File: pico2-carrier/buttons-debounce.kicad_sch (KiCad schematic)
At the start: 13 parts, among them SW5 BUT_L, SW6 BUT_M, SW7 BUT_R, U6 74HC14_x6

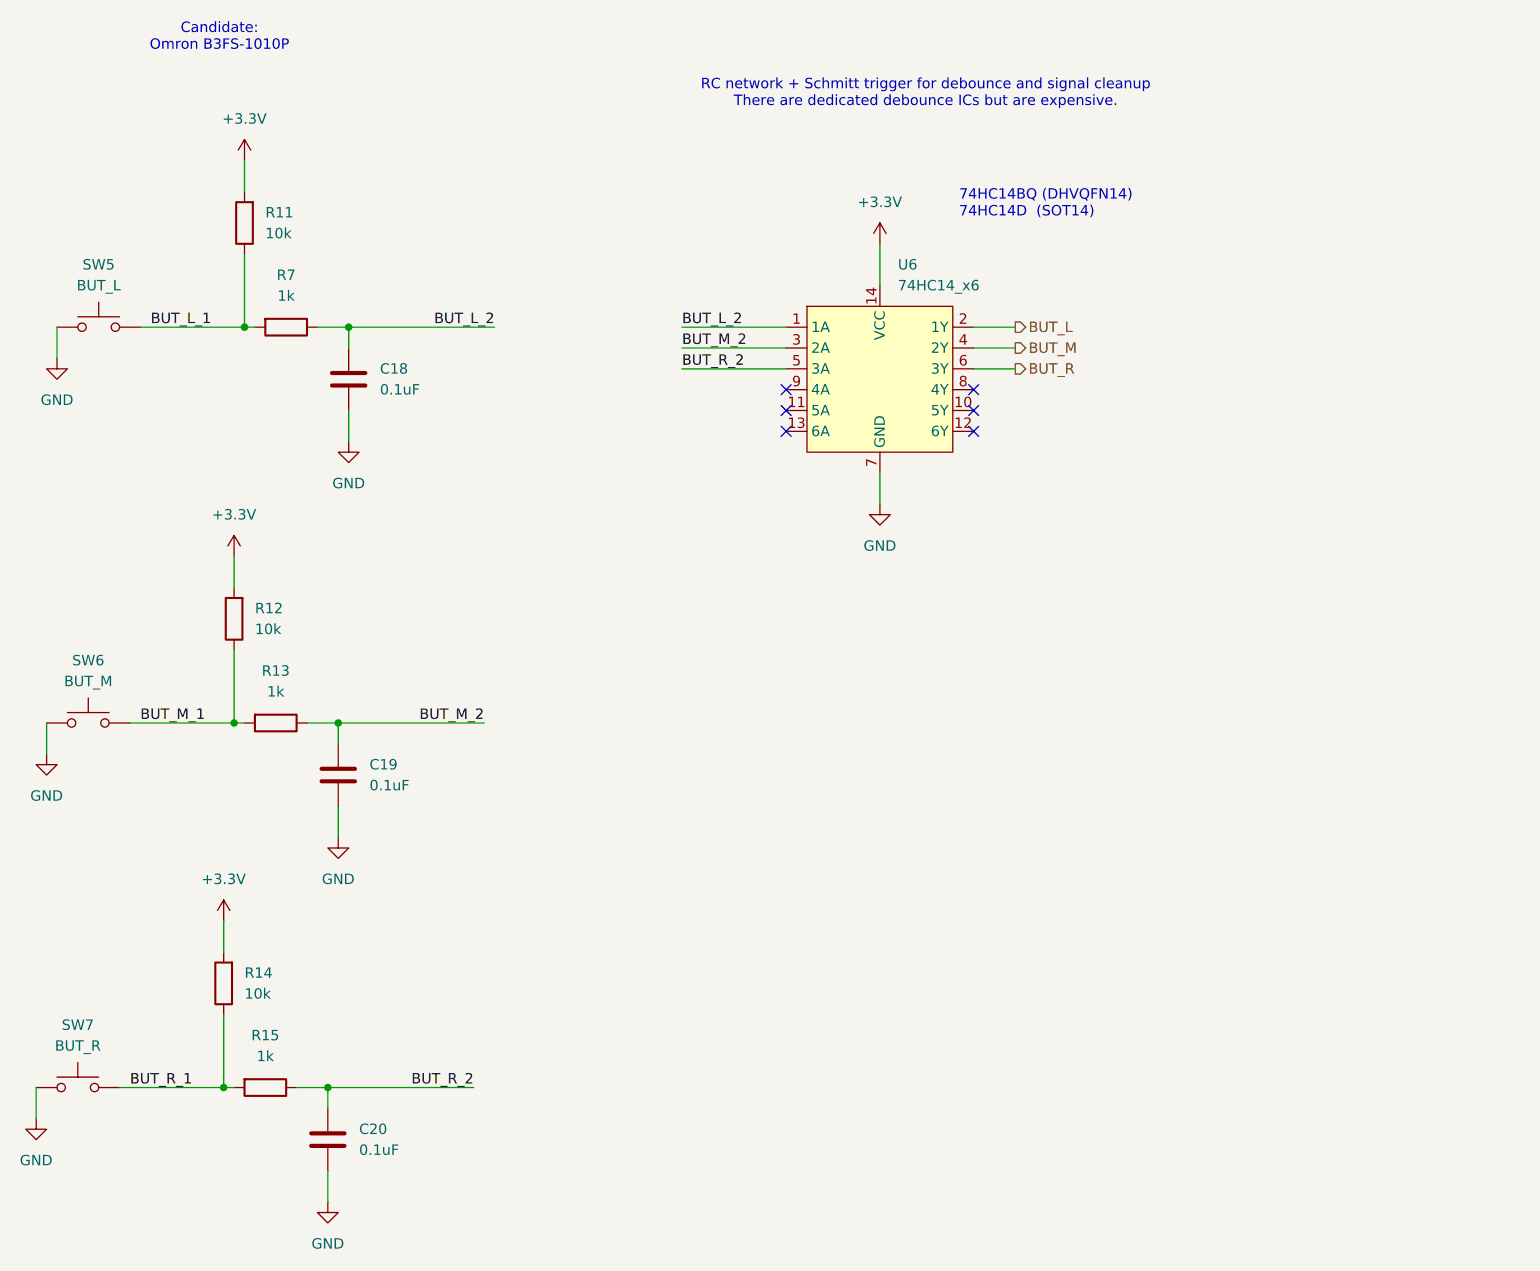
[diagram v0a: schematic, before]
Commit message: carrier: add 3.3V zone, start tidying buttons, update caps to 0603
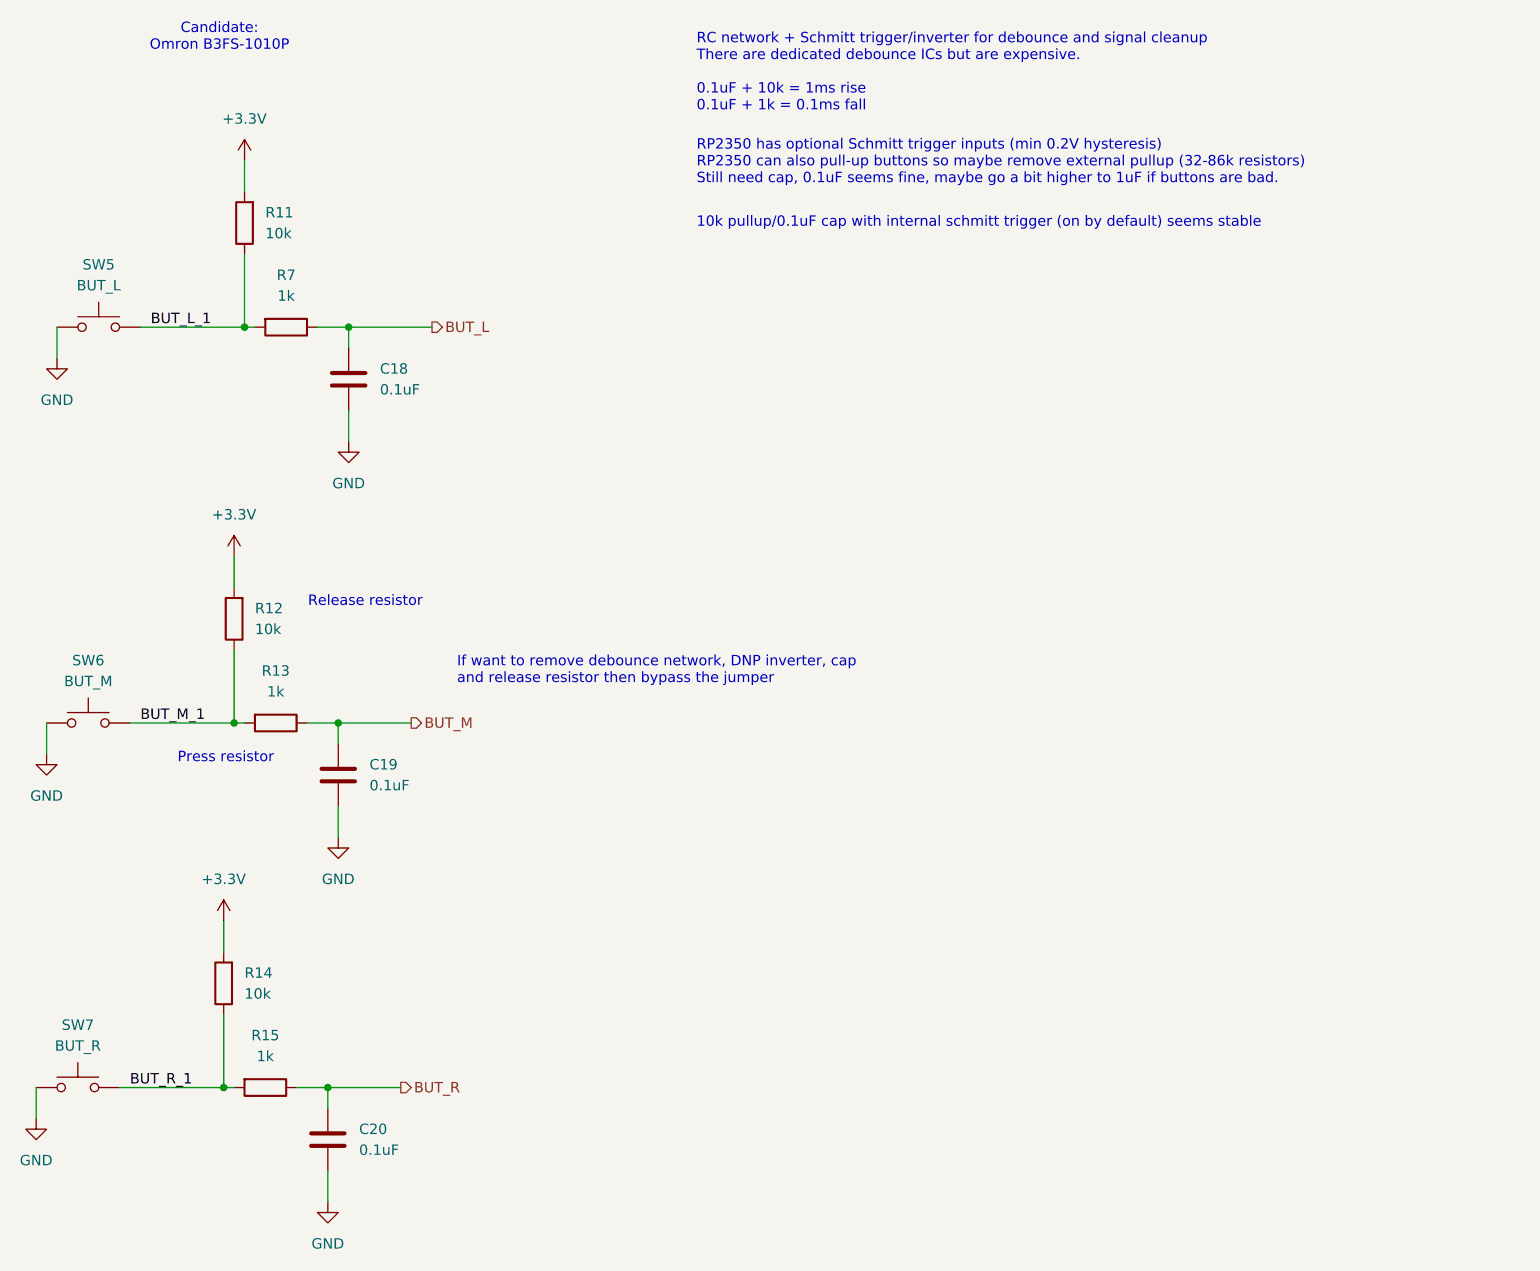
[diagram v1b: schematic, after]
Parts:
- removed U6: 74HC14_x6, symbol SamacSys_Parts:74HC14_x6
- C18, C19, C20, R7: footprint (none) -> Capacitor_SMD:C_0402_1005Metric
- R11, R12, R13, R14, R15: footprint (none) -> Resistor_SMD:R_0402_1005Metric
- SW5, SW6, SW7: footprint (none) -> Button_Switch_SMD:SW_SPST_Omron_B3FS-101xP
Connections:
- net BUT_L_2 is gone; now on net BUT_L: C18.1, R7.1
- net BUT_M_2 is gone; now on net BUT_M: C19.1, R13.1
- net BUT_R_2 is gone; now on net BUT_R: C20.1, R15.1
- no-connect marks 6 -> 0
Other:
- note added: "10k pullup/0.1uF cap with internal schmitt trigger (on by default) seems stable"
- note added: "If want to remove debounce network, DNP inverter, cap and release resistor then bypass the jumper"
- note added: "Press resistor"
- note added: "RC network + Schmitt trigger/inverter for debounce and signal cleanup There are dedicated debounce ICs but are expensive. 0.1uF + 10k = 1ms rise 0.1uF + 1k = 0.1ms fall"
- note added: "RP2350 has optional Schmitt trigger inputs (min 0.2V hysteresis) RP2350 can also pull-up buttons so maybe remove external pullup (32-86k resistors) Still need cap, 0.1uF seems fine, maybe go a bit higher to 1uF if buttons are bad."
- note added: "Release resistor"
- note removed: "74HC14BQ (DHVQFN14) 74HC14D (SOT14)"
- note removed: "RC network + Schmitt trigger for debounce and signal cleanup There are dedicated debounce ICs but are expensive."
